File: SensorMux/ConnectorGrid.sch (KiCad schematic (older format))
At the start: 253 parts

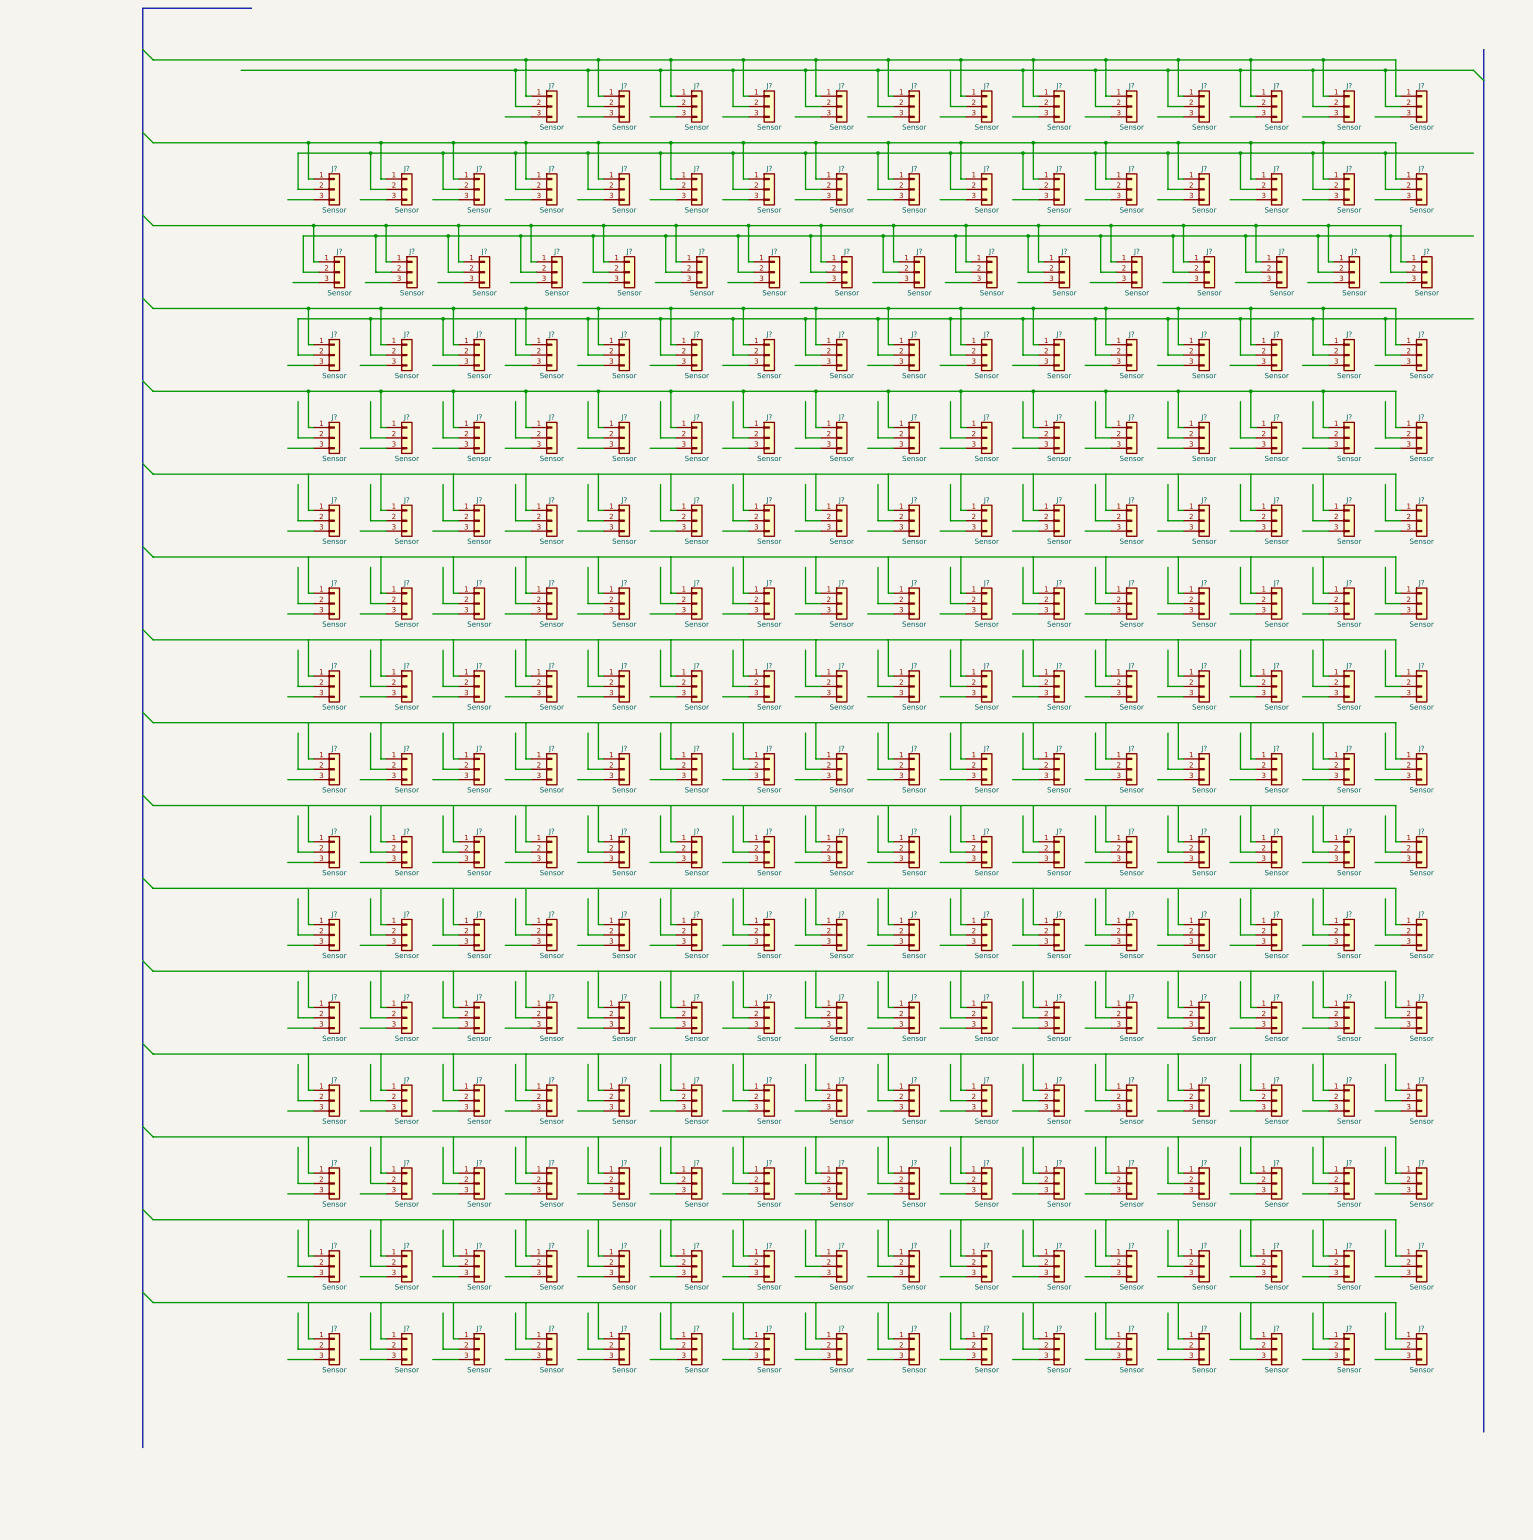
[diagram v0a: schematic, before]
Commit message: Added sensor grid schematics.
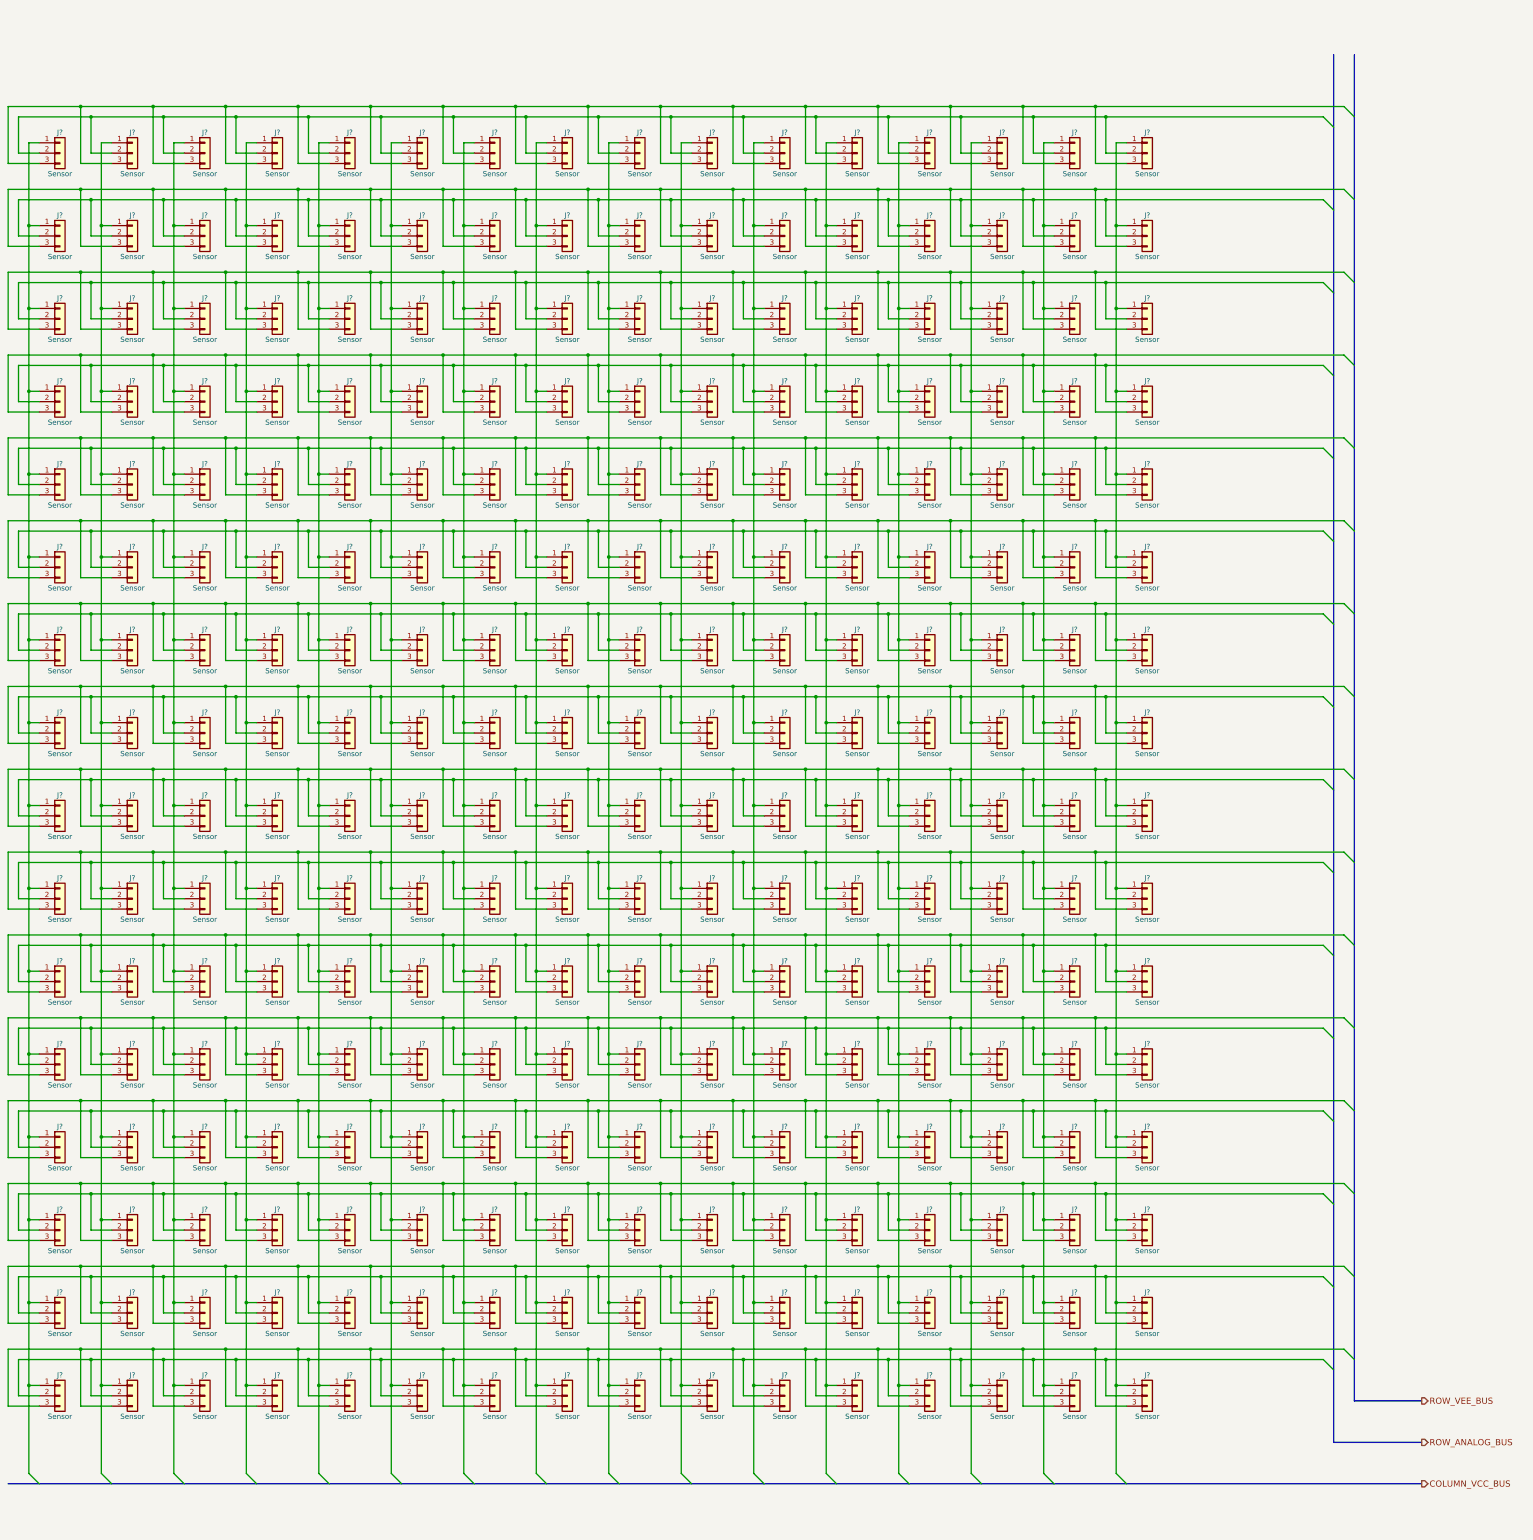
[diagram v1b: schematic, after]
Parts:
- removed J? (x253): Sensor, symbol Conn_01x03
- added J? (x256): Sensor, symbol Conn_01x03
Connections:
- net labels added: COLUMN_VCC_BUS, ROW_ANALOG_BUS, ROW_VEE_BUS
- wire segments 1285 -> 1328

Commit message: Added sensor wire  labels
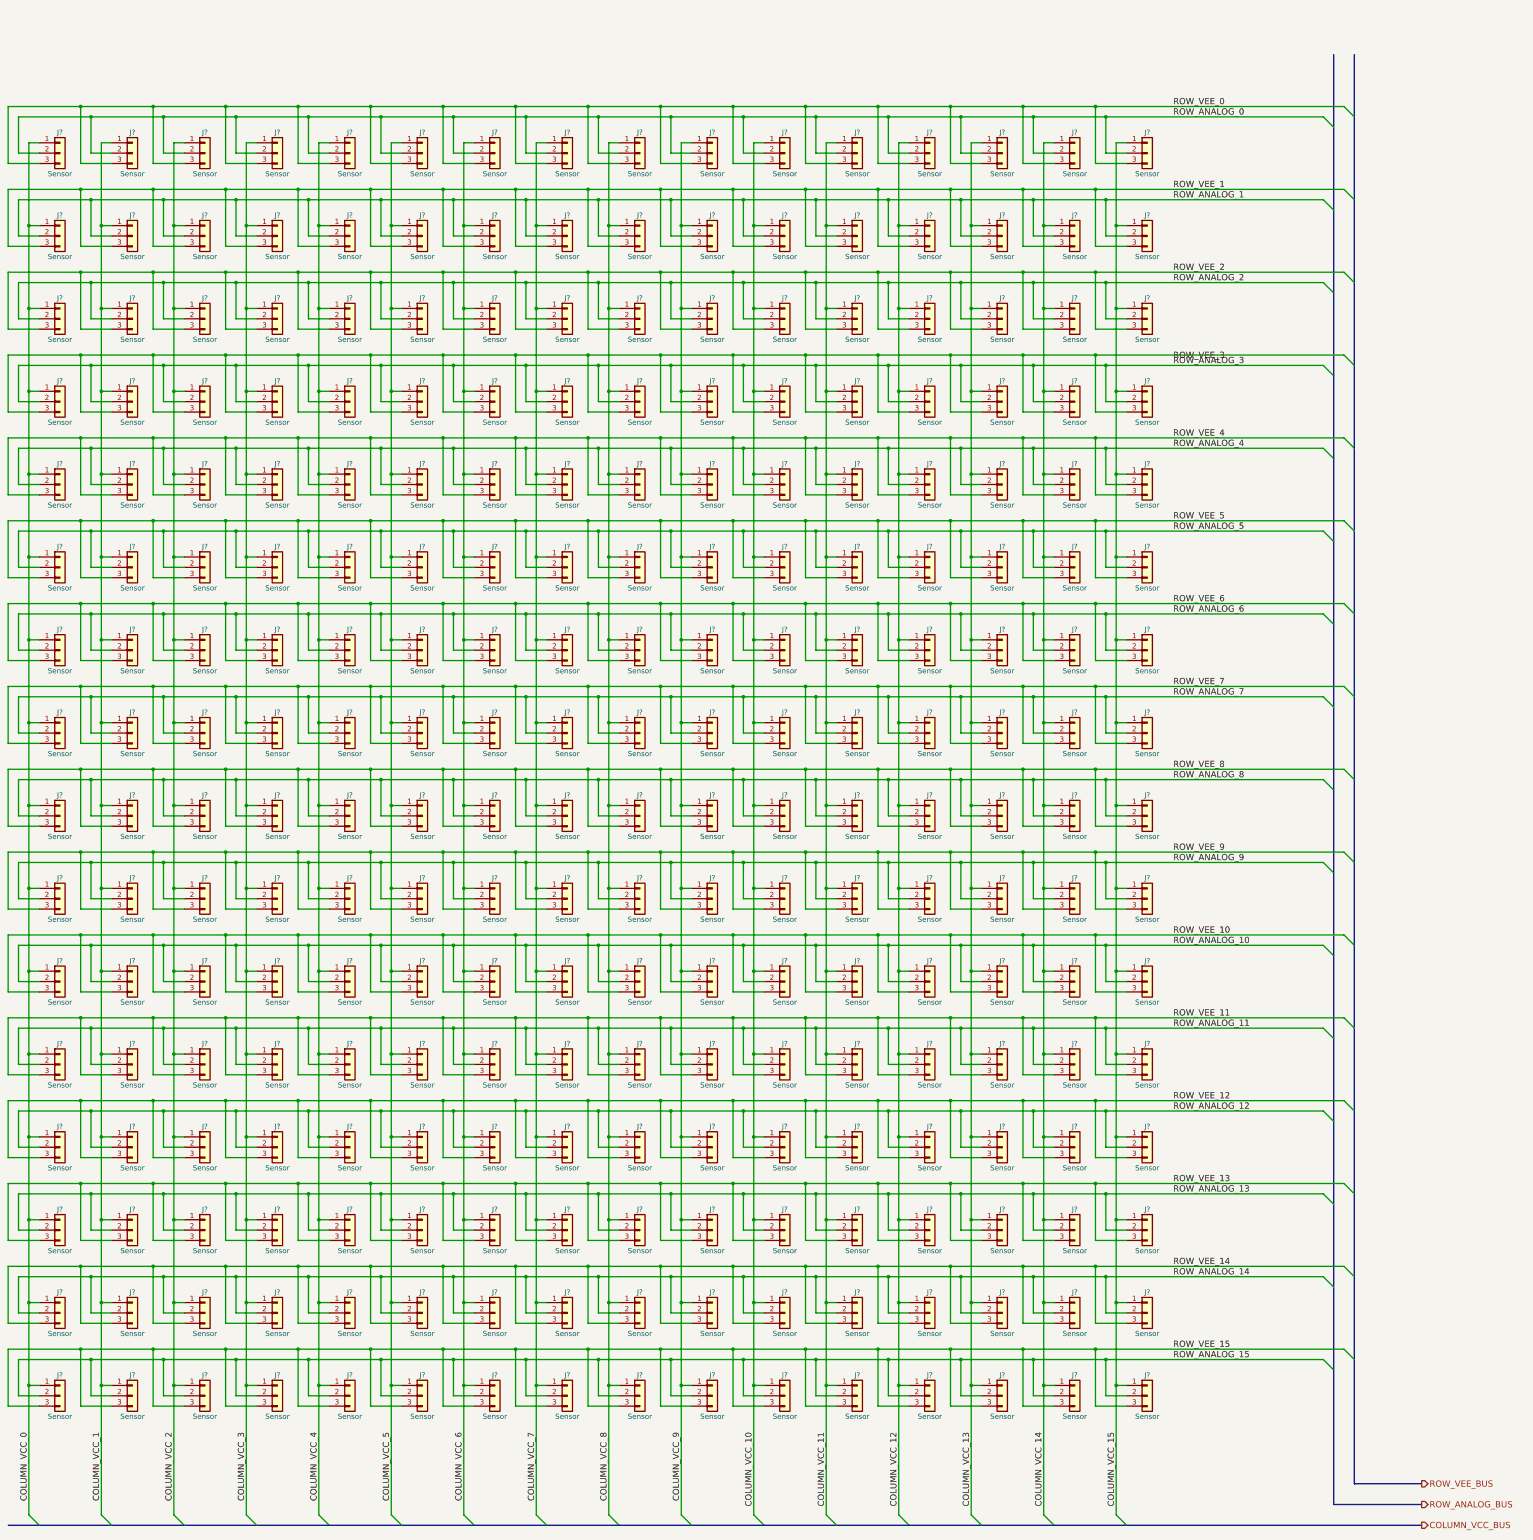
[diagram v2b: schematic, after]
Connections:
- net COLUMN_VCC_15: now reaches J?.1 (Pin_1), J?.1 (Pin_1), J?.1 (Pin_1), J?.1 (Pin_1), J?.1 (Pin_1), J?.1 (Pin_1), J?.1 (Pin_1), J?.1 (Pin_1), J?.1 (Pin_1), J?.1 (Pin_1), J?.1 (Pin_1), J?.1 (Pin_1), J?.1 (Pin_1), J?.1 (Pin_1), J?.1 (Pin_1), J?.1 (Pin_1)
- net ROW_ANALOG_15: now reaches J?.2 (Pin_2), J?.2 (Pin_2), J?.2 (Pin_2), J?.2 (Pin_2), J?.2 (Pin_2), J?.2 (Pin_2), J?.2 (Pin_2), J?.2 (Pin_2), J?.2 (Pin_2), J?.2 (Pin_2), J?.2 (Pin_2), J?.2 (Pin_2), J?.2 (Pin_2), J?.2 (Pin_2), J?.2 (Pin_2), J?.2 (Pin_2)
- net ROW_VEE_15: now reaches J?.3 (Pin_3), J?.3 (Pin_3), J?.3 (Pin_3), J?.3 (Pin_3), J?.3 (Pin_3), J?.3 (Pin_3), J?.3 (Pin_3), J?.3 (Pin_3), J?.3 (Pin_3), J?.3 (Pin_3), J?.3 (Pin_3), J?.3 (Pin_3), J?.3 (Pin_3), J?.3 (Pin_3), J?.3 (Pin_3), J?.3 (Pin_3)
- net COLUMN_VCC_14: now reaches J?.1 (Pin_1), J?.1 (Pin_1), J?.1 (Pin_1), J?.1 (Pin_1), J?.1 (Pin_1), J?.1 (Pin_1), J?.1 (Pin_1), J?.1 (Pin_1), J?.1 (Pin_1), J?.1 (Pin_1), J?.1 (Pin_1), J?.1 (Pin_1), J?.1 (Pin_1), J?.1 (Pin_1), J?.1 (Pin_1), J?.1 (Pin_1)
- net COLUMN_VCC_13: now reaches J?.1 (Pin_1), J?.1 (Pin_1), J?.1 (Pin_1), J?.1 (Pin_1), J?.1 (Pin_1), J?.1 (Pin_1), J?.1 (Pin_1), J?.1 (Pin_1), J?.1 (Pin_1), J?.1 (Pin_1), J?.1 (Pin_1), J?.1 (Pin_1), J?.1 (Pin_1), J?.1 (Pin_1), J?.1 (Pin_1), J?.1 (Pin_1)
- net COLUMN_VCC_12: now reaches J?.1 (Pin_1), J?.1 (Pin_1), J?.1 (Pin_1), J?.1 (Pin_1), J?.1 (Pin_1), J?.1 (Pin_1), J?.1 (Pin_1), J?.1 (Pin_1), J?.1 (Pin_1), J?.1 (Pin_1), J?.1 (Pin_1), J?.1 (Pin_1), J?.1 (Pin_1), J?.1 (Pin_1), J?.1 (Pin_1), J?.1 (Pin_1)
- net COLUMN_VCC_11: now reaches J?.1 (Pin_1), J?.1 (Pin_1), J?.1 (Pin_1), J?.1 (Pin_1), J?.1 (Pin_1), J?.1 (Pin_1), J?.1 (Pin_1), J?.1 (Pin_1), J?.1 (Pin_1), J?.1 (Pin_1), J?.1 (Pin_1), J?.1 (Pin_1), J?.1 (Pin_1), J?.1 (Pin_1), J?.1 (Pin_1), J?.1 (Pin_1)
- net COLUMN_VCC_10: now reaches J?.1 (Pin_1), J?.1 (Pin_1), J?.1 (Pin_1), J?.1 (Pin_1), J?.1 (Pin_1), J?.1 (Pin_1), J?.1 (Pin_1), J?.1 (Pin_1), J?.1 (Pin_1), J?.1 (Pin_1), J?.1 (Pin_1), J?.1 (Pin_1), J?.1 (Pin_1), J?.1 (Pin_1), J?.1 (Pin_1), J?.1 (Pin_1)
- net COLUMN_VCC_9: now reaches J?.1 (Pin_1), J?.1 (Pin_1), J?.1 (Pin_1), J?.1 (Pin_1), J?.1 (Pin_1), J?.1 (Pin_1), J?.1 (Pin_1), J?.1 (Pin_1), J?.1 (Pin_1), J?.1 (Pin_1), J?.1 (Pin_1), J?.1 (Pin_1), J?.1 (Pin_1), J?.1 (Pin_1), J?.1 (Pin_1), J?.1 (Pin_1)
- net COLUMN_VCC_8: now reaches J?.1 (Pin_1), J?.1 (Pin_1), J?.1 (Pin_1), J?.1 (Pin_1), J?.1 (Pin_1), J?.1 (Pin_1), J?.1 (Pin_1), J?.1 (Pin_1), J?.1 (Pin_1), J?.1 (Pin_1), J?.1 (Pin_1), J?.1 (Pin_1), J?.1 (Pin_1), J?.1 (Pin_1), J?.1 (Pin_1), J?.1 (Pin_1)
- net COLUMN_VCC_7: now reaches J?.1 (Pin_1), J?.1 (Pin_1), J?.1 (Pin_1), J?.1 (Pin_1), J?.1 (Pin_1), J?.1 (Pin_1), J?.1 (Pin_1), J?.1 (Pin_1), J?.1 (Pin_1), J?.1 (Pin_1), J?.1 (Pin_1), J?.1 (Pin_1), J?.1 (Pin_1), J?.1 (Pin_1), J?.1 (Pin_1), J?.1 (Pin_1)
- net COLUMN_VCC_6: now reaches J?.1 (Pin_1), J?.1 (Pin_1), J?.1 (Pin_1), J?.1 (Pin_1), J?.1 (Pin_1), J?.1 (Pin_1), J?.1 (Pin_1), J?.1 (Pin_1), J?.1 (Pin_1), J?.1 (Pin_1), J?.1 (Pin_1), J?.1 (Pin_1), J?.1 (Pin_1), J?.1 (Pin_1), J?.1 (Pin_1), J?.1 (Pin_1)
- net COLUMN_VCC_5: now reaches J?.1 (Pin_1), J?.1 (Pin_1), J?.1 (Pin_1), J?.1 (Pin_1), J?.1 (Pin_1), J?.1 (Pin_1), J?.1 (Pin_1), J?.1 (Pin_1), J?.1 (Pin_1), J?.1 (Pin_1), J?.1 (Pin_1), J?.1 (Pin_1), J?.1 (Pin_1), J?.1 (Pin_1), J?.1 (Pin_1), J?.1 (Pin_1)
- net COLUMN_VCC_4: now reaches J?.1 (Pin_1), J?.1 (Pin_1), J?.1 (Pin_1), J?.1 (Pin_1), J?.1 (Pin_1), J?.1 (Pin_1), J?.1 (Pin_1), J?.1 (Pin_1), J?.1 (Pin_1), J?.1 (Pin_1), J?.1 (Pin_1), J?.1 (Pin_1), J?.1 (Pin_1), J?.1 (Pin_1), J?.1 (Pin_1), J?.1 (Pin_1)
- net COLUMN_VCC_3: now reaches J?.1 (Pin_1), J?.1 (Pin_1), J?.1 (Pin_1), J?.1 (Pin_1), J?.1 (Pin_1), J?.1 (Pin_1), J?.1 (Pin_1), J?.1 (Pin_1), J?.1 (Pin_1), J?.1 (Pin_1), J?.1 (Pin_1), J?.1 (Pin_1), J?.1 (Pin_1), J?.1 (Pin_1), J?.1 (Pin_1), J?.1 (Pin_1)
- net COLUMN_VCC_2: now reaches J?.1 (Pin_1), J?.1 (Pin_1), J?.1 (Pin_1), J?.1 (Pin_1), J?.1 (Pin_1), J?.1 (Pin_1), J?.1 (Pin_1), J?.1 (Pin_1), J?.1 (Pin_1), J?.1 (Pin_1), J?.1 (Pin_1), J?.1 (Pin_1), J?.1 (Pin_1), J?.1 (Pin_1), J?.1 (Pin_1), J?.1 (Pin_1)
- net COLUMN_VCC_1: now reaches J?.1 (Pin_1), J?.1 (Pin_1), J?.1 (Pin_1), J?.1 (Pin_1), J?.1 (Pin_1), J?.1 (Pin_1), J?.1 (Pin_1), J?.1 (Pin_1), J?.1 (Pin_1), J?.1 (Pin_1), J?.1 (Pin_1), J?.1 (Pin_1), J?.1 (Pin_1), J?.1 (Pin_1), J?.1 (Pin_1), J?.1 (Pin_1)
- net COLUMN_VCC_0: now reaches J?.1 (Pin_1), J?.1 (Pin_1), J?.1 (Pin_1), J?.1 (Pin_1), J?.1 (Pin_1), J?.1 (Pin_1), J?.1 (Pin_1), J?.1 (Pin_1), J?.1 (Pin_1), J?.1 (Pin_1), J?.1 (Pin_1), J?.1 (Pin_1), J?.1 (Pin_1), J?.1 (Pin_1), J?.1 (Pin_1), J?.1 (Pin_1)
- net ROW_ANALOG_14: now reaches J?.2 (Pin_2), J?.2 (Pin_2), J?.2 (Pin_2), J?.2 (Pin_2), J?.2 (Pin_2), J?.2 (Pin_2), J?.2 (Pin_2), J?.2 (Pin_2), J?.2 (Pin_2), J?.2 (Pin_2), J?.2 (Pin_2), J?.2 (Pin_2), J?.2 (Pin_2), J?.2 (Pin_2), J?.2 (Pin_2), J?.2 (Pin_2)
- net ROW_VEE_14: now reaches J?.3 (Pin_3), J?.3 (Pin_3), J?.3 (Pin_3), J?.3 (Pin_3), J?.3 (Pin_3), J?.3 (Pin_3), J?.3 (Pin_3), J?.3 (Pin_3), J?.3 (Pin_3), J?.3 (Pin_3), J?.3 (Pin_3), J?.3 (Pin_3), J?.3 (Pin_3), J?.3 (Pin_3), J?.3 (Pin_3), J?.3 (Pin_3)
- net ROW_ANALOG_13: now reaches J?.2 (Pin_2), J?.2 (Pin_2), J?.2 (Pin_2), J?.2 (Pin_2), J?.2 (Pin_2), J?.2 (Pin_2), J?.2 (Pin_2), J?.2 (Pin_2), J?.2 (Pin_2), J?.2 (Pin_2), J?.2 (Pin_2), J?.2 (Pin_2), J?.2 (Pin_2), J?.2 (Pin_2), J?.2 (Pin_2), J?.2 (Pin_2)
- net ROW_VEE_13: now reaches J?.3 (Pin_3), J?.3 (Pin_3), J?.3 (Pin_3), J?.3 (Pin_3), J?.3 (Pin_3), J?.3 (Pin_3), J?.3 (Pin_3), J?.3 (Pin_3), J?.3 (Pin_3), J?.3 (Pin_3), J?.3 (Pin_3), J?.3 (Pin_3), J?.3 (Pin_3), J?.3 (Pin_3), J?.3 (Pin_3), J?.3 (Pin_3)
- net ROW_ANALOG_12: now reaches J?.2 (Pin_2), J?.2 (Pin_2), J?.2 (Pin_2), J?.2 (Pin_2), J?.2 (Pin_2), J?.2 (Pin_2), J?.2 (Pin_2), J?.2 (Pin_2), J?.2 (Pin_2), J?.2 (Pin_2), J?.2 (Pin_2), J?.2 (Pin_2), J?.2 (Pin_2), J?.2 (Pin_2), J?.2 (Pin_2), J?.2 (Pin_2)
- net ROW_VEE_12: now reaches J?.3 (Pin_3), J?.3 (Pin_3), J?.3 (Pin_3), J?.3 (Pin_3), J?.3 (Pin_3), J?.3 (Pin_3), J?.3 (Pin_3), J?.3 (Pin_3), J?.3 (Pin_3), J?.3 (Pin_3), J?.3 (Pin_3), J?.3 (Pin_3), J?.3 (Pin_3), J?.3 (Pin_3), J?.3 (Pin_3), J?.3 (Pin_3)
- net ROW_ANALOG_11: now reaches J?.2 (Pin_2), J?.2 (Pin_2), J?.2 (Pin_2), J?.2 (Pin_2), J?.2 (Pin_2), J?.2 (Pin_2), J?.2 (Pin_2), J?.2 (Pin_2), J?.2 (Pin_2), J?.2 (Pin_2), J?.2 (Pin_2), J?.2 (Pin_2), J?.2 (Pin_2), J?.2 (Pin_2), J?.2 (Pin_2), J?.2 (Pin_2)
- net ROW_VEE_11: now reaches J?.3 (Pin_3), J?.3 (Pin_3), J?.3 (Pin_3), J?.3 (Pin_3), J?.3 (Pin_3), J?.3 (Pin_3), J?.3 (Pin_3), J?.3 (Pin_3), J?.3 (Pin_3), J?.3 (Pin_3), J?.3 (Pin_3), J?.3 (Pin_3), J?.3 (Pin_3), J?.3 (Pin_3), J?.3 (Pin_3), J?.3 (Pin_3)
- net ROW_ANALOG_10: now reaches J?.2 (Pin_2), J?.2 (Pin_2), J?.2 (Pin_2), J?.2 (Pin_2), J?.2 (Pin_2), J?.2 (Pin_2), J?.2 (Pin_2), J?.2 (Pin_2), J?.2 (Pin_2), J?.2 (Pin_2), J?.2 (Pin_2), J?.2 (Pin_2), J?.2 (Pin_2), J?.2 (Pin_2), J?.2 (Pin_2), J?.2 (Pin_2)
- net ROW_VEE_10: now reaches J?.3 (Pin_3), J?.3 (Pin_3), J?.3 (Pin_3), J?.3 (Pin_3), J?.3 (Pin_3), J?.3 (Pin_3), J?.3 (Pin_3), J?.3 (Pin_3), J?.3 (Pin_3), J?.3 (Pin_3), J?.3 (Pin_3), J?.3 (Pin_3), J?.3 (Pin_3), J?.3 (Pin_3), J?.3 (Pin_3), J?.3 (Pin_3)
- net ROW_ANALOG_9: now reaches J?.2 (Pin_2), J?.2 (Pin_2), J?.2 (Pin_2), J?.2 (Pin_2), J?.2 (Pin_2), J?.2 (Pin_2), J?.2 (Pin_2), J?.2 (Pin_2), J?.2 (Pin_2), J?.2 (Pin_2), J?.2 (Pin_2), J?.2 (Pin_2), J?.2 (Pin_2), J?.2 (Pin_2), J?.2 (Pin_2), J?.2 (Pin_2)
- net ROW_VEE_9: now reaches J?.3 (Pin_3), J?.3 (Pin_3), J?.3 (Pin_3), J?.3 (Pin_3), J?.3 (Pin_3), J?.3 (Pin_3), J?.3 (Pin_3), J?.3 (Pin_3), J?.3 (Pin_3), J?.3 (Pin_3), J?.3 (Pin_3), J?.3 (Pin_3), J?.3 (Pin_3), J?.3 (Pin_3), J?.3 (Pin_3), J?.3 (Pin_3)
- net ROW_ANALOG_8: now reaches J?.2 (Pin_2), J?.2 (Pin_2), J?.2 (Pin_2), J?.2 (Pin_2), J?.2 (Pin_2), J?.2 (Pin_2), J?.2 (Pin_2), J?.2 (Pin_2), J?.2 (Pin_2), J?.2 (Pin_2), J?.2 (Pin_2), J?.2 (Pin_2), J?.2 (Pin_2), J?.2 (Pin_2), J?.2 (Pin_2), J?.2 (Pin_2)
- net ROW_VEE_8: now reaches J?.3 (Pin_3), J?.3 (Pin_3), J?.3 (Pin_3), J?.3 (Pin_3), J?.3 (Pin_3), J?.3 (Pin_3), J?.3 (Pin_3), J?.3 (Pin_3), J?.3 (Pin_3), J?.3 (Pin_3), J?.3 (Pin_3), J?.3 (Pin_3), J?.3 (Pin_3), J?.3 (Pin_3), J?.3 (Pin_3), J?.3 (Pin_3)
- net ROW_ANALOG_7: now reaches J?.2 (Pin_2), J?.2 (Pin_2), J?.2 (Pin_2), J?.2 (Pin_2), J?.2 (Pin_2), J?.2 (Pin_2), J?.2 (Pin_2), J?.2 (Pin_2), J?.2 (Pin_2), J?.2 (Pin_2), J?.2 (Pin_2), J?.2 (Pin_2), J?.2 (Pin_2), J?.2 (Pin_2), J?.2 (Pin_2), J?.2 (Pin_2)
- net ROW_VEE_7: now reaches J?.3 (Pin_3), J?.3 (Pin_3), J?.3 (Pin_3), J?.3 (Pin_3), J?.3 (Pin_3), J?.3 (Pin_3), J?.3 (Pin_3), J?.3 (Pin_3), J?.3 (Pin_3), J?.3 (Pin_3), J?.3 (Pin_3), J?.3 (Pin_3), J?.3 (Pin_3), J?.3 (Pin_3), J?.3 (Pin_3), J?.3 (Pin_3)
- net ROW_ANALOG_6: now reaches J?.2 (Pin_2), J?.2 (Pin_2), J?.2 (Pin_2), J?.2 (Pin_2), J?.2 (Pin_2), J?.2 (Pin_2), J?.2 (Pin_2), J?.2 (Pin_2), J?.2 (Pin_2), J?.2 (Pin_2), J?.2 (Pin_2), J?.2 (Pin_2), J?.2 (Pin_2), J?.2 (Pin_2), J?.2 (Pin_2), J?.2 (Pin_2)
- net ROW_VEE_6: now reaches J?.3 (Pin_3), J?.3 (Pin_3), J?.3 (Pin_3), J?.3 (Pin_3), J?.3 (Pin_3), J?.3 (Pin_3), J?.3 (Pin_3), J?.3 (Pin_3), J?.3 (Pin_3), J?.3 (Pin_3), J?.3 (Pin_3), J?.3 (Pin_3), J?.3 (Pin_3), J?.3 (Pin_3), J?.3 (Pin_3), J?.3 (Pin_3)
- net ROW_ANALOG_5: now reaches J?.2 (Pin_2), J?.2 (Pin_2), J?.2 (Pin_2), J?.2 (Pin_2), J?.2 (Pin_2), J?.2 (Pin_2), J?.2 (Pin_2), J?.2 (Pin_2), J?.2 (Pin_2), J?.2 (Pin_2), J?.2 (Pin_2), J?.2 (Pin_2), J?.2 (Pin_2), J?.2 (Pin_2), J?.2 (Pin_2), J?.2 (Pin_2)
- net ROW_VEE_5: now reaches J?.3 (Pin_3), J?.3 (Pin_3), J?.3 (Pin_3), J?.3 (Pin_3), J?.3 (Pin_3), J?.3 (Pin_3), J?.3 (Pin_3), J?.3 (Pin_3), J?.3 (Pin_3), J?.3 (Pin_3), J?.3 (Pin_3), J?.3 (Pin_3), J?.3 (Pin_3), J?.3 (Pin_3), J?.3 (Pin_3), J?.3 (Pin_3)
- net ROW_ANALOG_4: now reaches J?.2 (Pin_2), J?.2 (Pin_2), J?.2 (Pin_2), J?.2 (Pin_2), J?.2 (Pin_2), J?.2 (Pin_2), J?.2 (Pin_2), J?.2 (Pin_2), J?.2 (Pin_2), J?.2 (Pin_2), J?.2 (Pin_2), J?.2 (Pin_2), J?.2 (Pin_2), J?.2 (Pin_2), J?.2 (Pin_2), J?.2 (Pin_2)
- net ROW_VEE_4: now reaches J?.3 (Pin_3), J?.3 (Pin_3), J?.3 (Pin_3), J?.3 (Pin_3), J?.3 (Pin_3), J?.3 (Pin_3), J?.3 (Pin_3), J?.3 (Pin_3), J?.3 (Pin_3), J?.3 (Pin_3), J?.3 (Pin_3), J?.3 (Pin_3), J?.3 (Pin_3), J?.3 (Pin_3), J?.3 (Pin_3), J?.3 (Pin_3)
- net ROW_ANALOG_3: now reaches J?.2 (Pin_2), J?.2 (Pin_2), J?.2 (Pin_2), J?.2 (Pin_2), J?.2 (Pin_2), J?.2 (Pin_2), J?.2 (Pin_2), J?.2 (Pin_2), J?.2 (Pin_2), J?.2 (Pin_2), J?.2 (Pin_2), J?.2 (Pin_2), J?.2 (Pin_2), J?.2 (Pin_2), J?.2 (Pin_2), J?.2 (Pin_2)
- net ROW_ANALOG_2: now reaches J?.2 (Pin_2), J?.2 (Pin_2), J?.2 (Pin_2), J?.2 (Pin_2), J?.2 (Pin_2), J?.2 (Pin_2), J?.2 (Pin_2), J?.2 (Pin_2), J?.2 (Pin_2), J?.2 (Pin_2), J?.2 (Pin_2), J?.2 (Pin_2), J?.2 (Pin_2), J?.2 (Pin_2), J?.2 (Pin_2), J?.2 (Pin_2)
- net ROW_VEE_2: now reaches J?.3 (Pin_3), J?.3 (Pin_3), J?.3 (Pin_3), J?.3 (Pin_3), J?.3 (Pin_3), J?.3 (Pin_3), J?.3 (Pin_3), J?.3 (Pin_3), J?.3 (Pin_3), J?.3 (Pin_3), J?.3 (Pin_3), J?.3 (Pin_3), J?.3 (Pin_3), J?.3 (Pin_3), J?.3 (Pin_3), J?.3 (Pin_3)
- net ROW_ANALOG_1: now reaches J?.2 (Pin_2), J?.2 (Pin_2), J?.2 (Pin_2), J?.2 (Pin_2), J?.2 (Pin_2), J?.2 (Pin_2), J?.2 (Pin_2), J?.2 (Pin_2), J?.2 (Pin_2), J?.2 (Pin_2), J?.2 (Pin_2), J?.2 (Pin_2), J?.2 (Pin_2), J?.2 (Pin_2), J?.2 (Pin_2), J?.2 (Pin_2)
- net ROW_VEE_1: now reaches J?.3 (Pin_3), J?.3 (Pin_3), J?.3 (Pin_3), J?.3 (Pin_3), J?.3 (Pin_3), J?.3 (Pin_3), J?.3 (Pin_3), J?.3 (Pin_3), J?.3 (Pin_3), J?.3 (Pin_3), J?.3 (Pin_3), J?.3 (Pin_3), J?.3 (Pin_3), J?.3 (Pin_3), J?.3 (Pin_3), J?.3 (Pin_3)
- net ROW_ANALOG_0: now reaches J?.2 (Pin_2), J?.2 (Pin_2), J?.2 (Pin_2), J?.2 (Pin_2), J?.2 (Pin_2), J?.2 (Pin_2), J?.2 (Pin_2), J?.2 (Pin_2), J?.2 (Pin_2), J?.2 (Pin_2), J?.2 (Pin_2), J?.2 (Pin_2), J?.2 (Pin_2), J?.2 (Pin_2), J?.2 (Pin_2), J?.2 (Pin_2)
- net ROW_VEE_0: now reaches J?.3 (Pin_3), J?.3 (Pin_3), J?.3 (Pin_3), J?.3 (Pin_3), J?.3 (Pin_3), J?.3 (Pin_3), J?.3 (Pin_3), J?.3 (Pin_3), J?.3 (Pin_3), J?.3 (Pin_3), J?.3 (Pin_3), J?.3 (Pin_3), J?.3 (Pin_3), J?.3 (Pin_3), J?.3 (Pin_3), J?.3 (Pin_3)
